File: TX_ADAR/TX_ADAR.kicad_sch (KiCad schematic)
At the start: 8 parts, among them SW2 SW_SPDT, U2 ADAR2001ACCZ

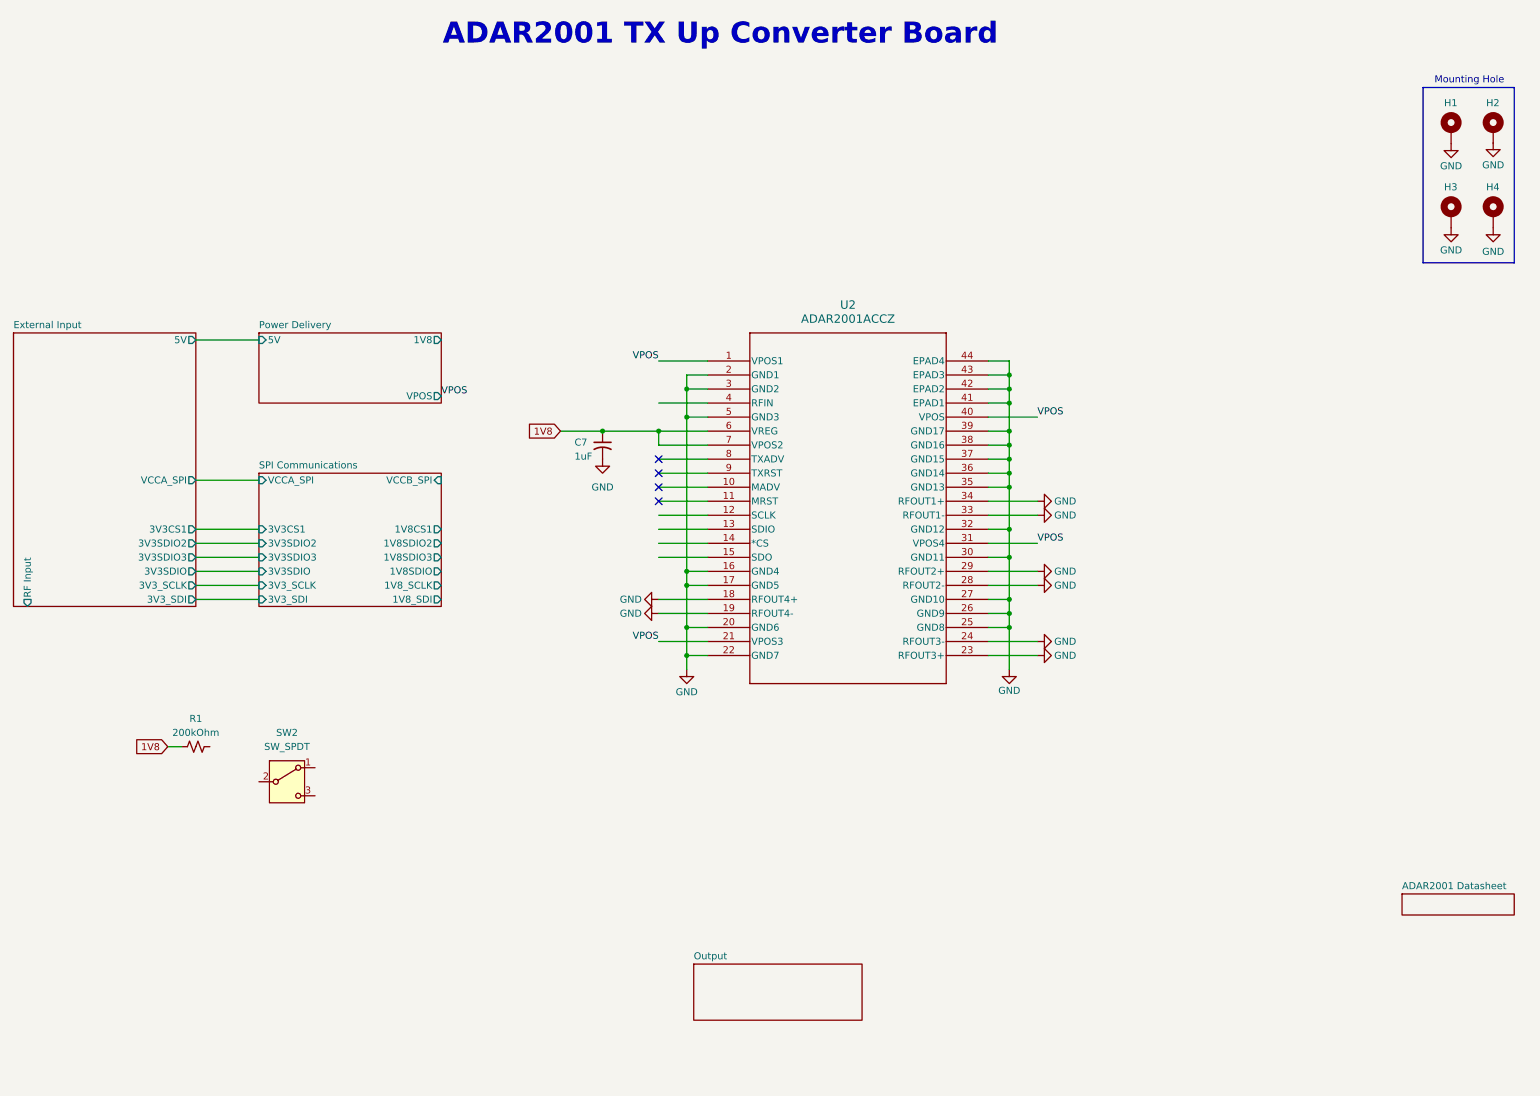
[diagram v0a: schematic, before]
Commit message: Cleaning up schematic
Added Cal Line
Connected RFOuts to connectors
Worked on State Machine connections
Finished connecting SDP Connector (need to double check)
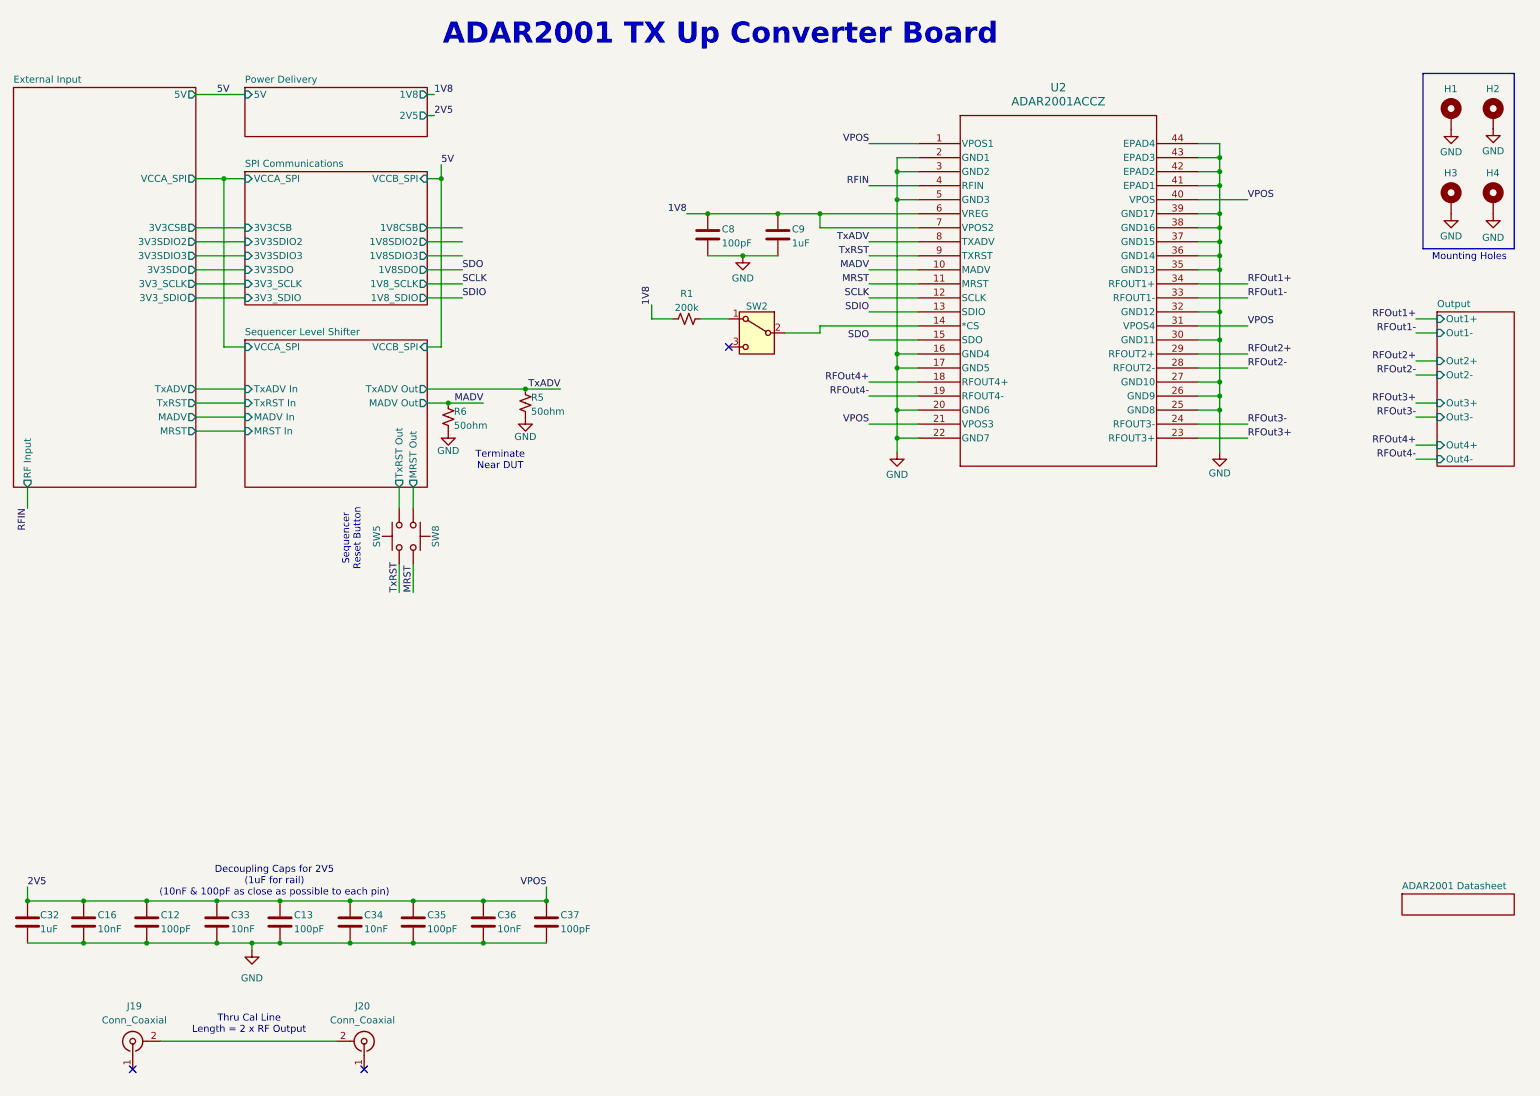
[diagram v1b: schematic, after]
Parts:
- removed C7: 1uF, symbol Device:C_Small_US
- added C12, C13, C35, C37, C8: 100pF, symbol Device:C
- added C16, C33, C34, C36: 10nF, symbol Device:C
- added C32, C9: 1uF, symbol Device:C
- added J19, J20: Conn_Coaxial, symbol Connector:Conn_Coaxial
- added R5, R6: 50ohm, Resistor_THT:R_Array_SIP4, symbol Device:R_Small_US
- added SW5, SW8: SW_Push, Package_TO_SOT_THT:TO-220-3_Vertical, symbol Switch:SW_Push
- R1: value 200kOhm -> 200k
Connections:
- net 1V8: now also R1.2, C8.1, C9.1; no longer R1.1
- net GND: now also C12.2, C13.2, C16.2, C32.2, C33.2, C34.2, C35.2, C36.2, C37.2, C8.2, C9.2, R5.2, R6.2; no longer U2.18 (RFOUT4+), U2.19 (RFOUT4-), U2.23 (RFOUT3+), U2.24 (RFOUT3-), U2.28 (RFOUT2-), U2.29 (RFOUT2+), U2.33 (RFOUT1-), U2.34 (RFOUT1+)
- net MADV: now reaches U2.10 (MADV)
- net MADV: now also R6.1
- net MRST: now reaches U2.11 (MRST)
- net MRST: now also SW8.2
- net SCLK: now reaches U2.12 (SCLK)
- net SDIO: now reaches U2.13 (SDIO)
- net at U2.14 (*CS): now also SW2.2 (B)
- net SDO: now reaches U2.15 (SDO)
- net RFIN: now reaches U2.4 (RFIN)
- net TxADV: now reaches U2.8 (TXADV)
- net TxADV: now also R5.1
- net TxRST: now reaches U2.9 (TXRST)
- net TxRST: now also SW5.1
- net at SW2.1 (A): now also R1.1
- net VPOS renamed 2V5
- net 2V5: now also C12.1, C13.1, C16.1, C32.1, C33.1, C34.1, C35.1, C36.1, C37.1
- new net: J19.2 (Ext), J20.2 (Ext)
- new net RFOut1+: U2.34 (RFOUT1+)
- new net RFOut1-: U2.33 (RFOUT1-)
- new net RFOut2+: U2.29 (RFOUT2+)
- new net RFOut2-: U2.28 (RFOUT2-)
- new net RFOut3+: U2.23 (RFOUT3+)
- new net RFOut3-: U2.24 (RFOUT3-)
- new net RFOut4+: U2.18 (RFOUT4+)
- new net RFOut4-: U2.19 (RFOUT4-)
- new net Sequencer Level Shifter/MRST Out: SW8.1
- new net Sequencer Level Shifter/TxRST Out: SW5.2
- no-connect marks 4 -> 3
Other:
- added sheet Sequencer Level Shifter (SequencerLevelShifter.kicad_sch)
- sheet External Input ports: added 3V3CSB, 3V3SDO, 3V3_SDIO, MADV, MRST, TxADV, TxRST; removed 3V3CS1, 3V3SDIO, 3V3_SDI
- sheet Output ports: added Out1+, Out1-, Out2+, Out2-, Out3+, Out3-, Out4+, Out4-; removed none
- sheet Power Delivery ports: added 2V5; removed VPOS
- sheet SPI Communications ports: added 1V8CSB, 1V8SDO, 1V8_SDIO, 3V3CSB, 3V3SDO, 3V3_SDIO; removed 1V8CS1, 1V8SDIO, 1V8_SDI, 3V3CS1, 3V3SDIO, 3V3_SDI
- note added: "Decoupling Caps for 2V5 (1uF for rail) (10nF & 100pF as close as possible to each pin)"
- note added: "Mounting Holes"
- note added: "Sequencer Reset Button"
- note added: "Terminate Near DUT"
- note added: "Thru Cal Line Length = 2 x RF Output"
- note removed: "Mounting Hole"
- moved on the sheet: H1, H2, H3, H4, SW2, U2

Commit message: Running ERC
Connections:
- net GND: now also H2.1
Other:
- sheet SPI Communications ports: added 1V8_SDI, 3V3_SDI; removed 1V8_SDIO, 3V3_SDIO
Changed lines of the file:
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@@
 	(symbol
 		(lib_id "power:GND")
-		(at 280.67 22.6825 0)
+		(at 280.67 22.86 0)
 		(unit 1)
 		(body_style 1)
@@
 		(dnp no)
 		(property "Reference" "#PWR019"
-			(at 280.67 29.0325 0)
+			(at 280.67 29.21 0)
 			(hide yes)
 			(show_name no)
@@
 		)
 		(property "Value" "GND"
-			(at 280.67 26.7465 0)
+			(at 280.67 26.924 0)
 			(show_name no)
 			(do_not_autoplace no)
@@
 		)
 		(property "Footprint" ""
-			(at 280.67 22.6825 0)
-			(hide yes)
-			(show_name no)
-			(do_not_autoplace no)
-			(effects
-				(font
-					(size 1.27 1.27)
-				)
-			)
-		)
-		(property "Datasheet" ""
-			(at 280.67 22.6825 0)
+			(at 280.67 22.86 0)
+			(hide yes)
+			(show_name no)
+			(do_not_autoplace no)
+			(effects
+				(font
+					(size 1.27 1.27)
+				)
+			)
+		)
+		(property "Datasheet" ""
+			(at 280.67 22.86 0)
 			(hide yes)
 			(show_name no)
@@
 		)
 		(property "Description" "Power symbol creates a global label with name \"GND\" , ground"
-			(at 280.67 22.6825 0)
+			(at 280.67 22.86 0)
 			(hide yes)
 			(show_name no)
@@
 			)
 		)
-		(pin "1V8_SDIO" output
+		(pin "1V8_SDI" output
 			(at 87.63 53.34 0)
 			(effects
@@
 			)
 		)
-		(pin "3V3_SDIO" input
+		(pin "3V3_SDI" input
 			(at 54.61 53.34 180)
 			(effects

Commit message: Fixing problems pointed out
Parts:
- removed R1: 200k, symbol Device:R_Small_US
- removed SW2: SW_SPDT, symbol Switch:SW_SPDT
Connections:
- net GND: now also J19.1 (In), J20.1 (In)
- net CSB: now reaches U2.14 (*CS)
- no-connect marks 3 -> 2
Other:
- sheet External Input ports: added 3V3_VCCB_SPI; removed VCCA_SPI
- moved on the sheet: J19, J20

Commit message: Fixed more issues
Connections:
- net GND: now also J19.2 (Ext), J20.2 (Ext); no longer J19.1 (In), J20.1 (In)
- net 1V8 renamed +1V8
- net 2V5 renamed +2V5
- new net: J19.1 (In), J20.1 (In)
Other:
- sheet External Input ports: added none; removed 5V
- sheet Power Delivery ports: added none; removed 1V8, 2V5, 5V
- moved on the sheet: C12, C13, C16, C32, C33, C34, C35, C36, C37, J19, J20
